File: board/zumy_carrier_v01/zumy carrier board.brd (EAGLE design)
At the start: 54 x 88.9 mm, 24 parts, among them IC1 SN74AUP2G17, IC2 SN74AUP2G17, J1 ODROID_POWER, J2 BATT_POWER, M1 POLOLU_STEP_DOWN, M2 ITG/MPU_MODULE, M3 POLOLU_DRV8833_MODULE, SW1 500SSP1S1M6QEA

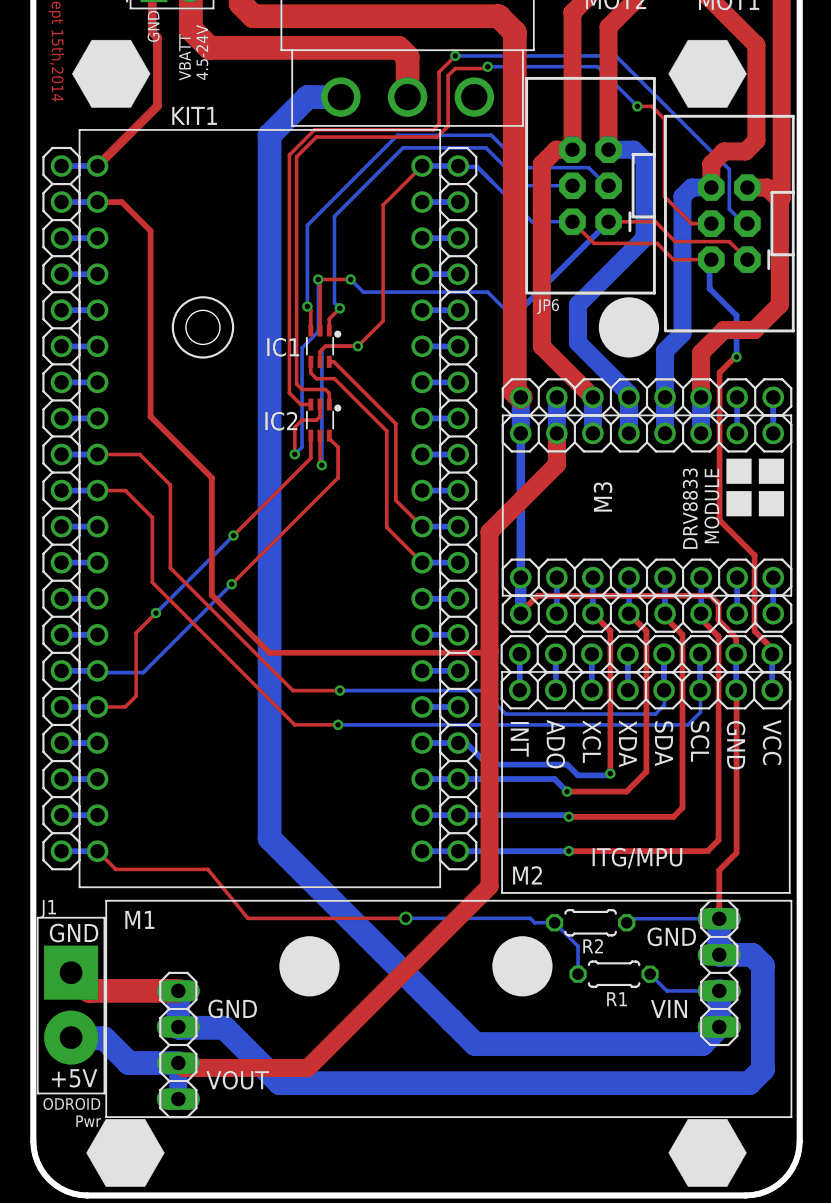
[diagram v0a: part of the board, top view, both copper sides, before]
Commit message: Added Rev. E Parts (5V Reg with UVLO, Cap on vsense, caps on level translators). Before ripup and rearrange.
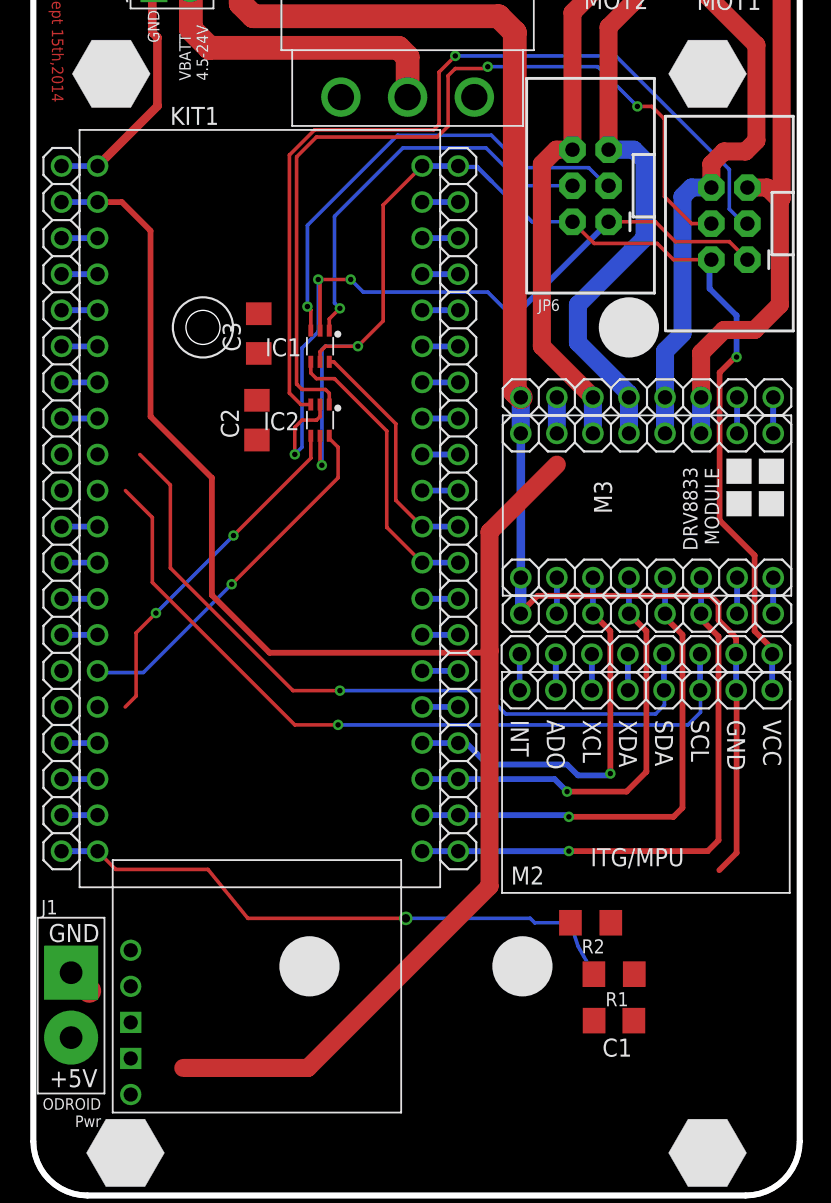
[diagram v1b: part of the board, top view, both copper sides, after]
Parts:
- removed M1: POLOLU_STEP_DOWN, zumy:POLOLU_STEP_DOWN
- added C1, C2, C3: 0.1uF, rcl:C1206
- added U$5: POLOLU_D24V50F5, zumy:POLOLU_D24V50F5
- R1: value (none) -> 200k; device resistor:0204/5 -> resistor:R1206
- R2: value (none) -> 100k; device resistor:0204/5 -> resistor:R1206
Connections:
- removed net N$35: JP5.7, KIT1.P$27
- removed net N$36: JP5.8, KIT1.P$28
- removed net N$39: JP5.11, KIT1.D+
- removed net N$40: JP5.12, KIT1.D-
- new net N$10: JP4.16, KIT1.P$16
- new net N$7: JP4.9, KIT1.P$9
- new net N$8: JP4.10, KIT1.P$10
- new net N$9: JP4.15, KIT1.P$15
- net +3V3: now also C2.1, C3.1
- net +5V: now also U$5.VOUT; no longer JP3.2, M1.VOUT1, M1.VOUT2, M3.VIN
- net GND: now also C1.2, C2.2, C3.2, U$5.GND1, U$5.GND2; no longer M1.GND1, M1.GND2, M1.GND3, M1.GND4
- net M2_ENCA_DIG: now also JP5.12, KIT1.D-; no longer JP4.15, KIT1.P$15
- net M2_ENCB_DIG: now also JP5.11, KIT1.D+; no longer JP4.16, KIT1.P$16
- net MPU_SCL: now also JP5.7, KIT1.P$27; no longer JP4.10, KIT1.P$10
- net MPU_SDA: now also JP5.8, KIT1.P$28; no longer JP4.9, KIT1.P$9
- net SW_VBATT: now also JP3.2, M3.VIN, U$5.VIN; no longer M1.VIN1, M1.VIN2
- net V_BATT_SENSE: now also C1.1
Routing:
- net SW_VBATT: track 102.4 -> 2.63 mm
- net GND: track 263.8 -> 188.5 mm
- net +5V: track 130.5 -> 114.4 mm
- net MPU_SDA: track 57.5 -> 54.3 mm
- net N$40: track 2.54 -> 0.00 mm
- net N$39: track 2.54 -> 0.00 mm
- net N$36: track 2.54 -> 0.00 mm
- net N$35: track 2.54 -> 0.00 mm
- net MPU_SCL: track 59.2 -> 57.0 mm
- net M2_ENCB_DIG: track 29.0 -> 27.1 mm
- net V_BATT_SENSE: track 41.3 -> 42.1 mm
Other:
- board text added: "A. Pullin A.J. Chen A.D. Buchan 2015"
- board text added: "Rev E"
- board text removed: "A. Pullin A.J. Chen 2014"
- board text removed: "Rev D"

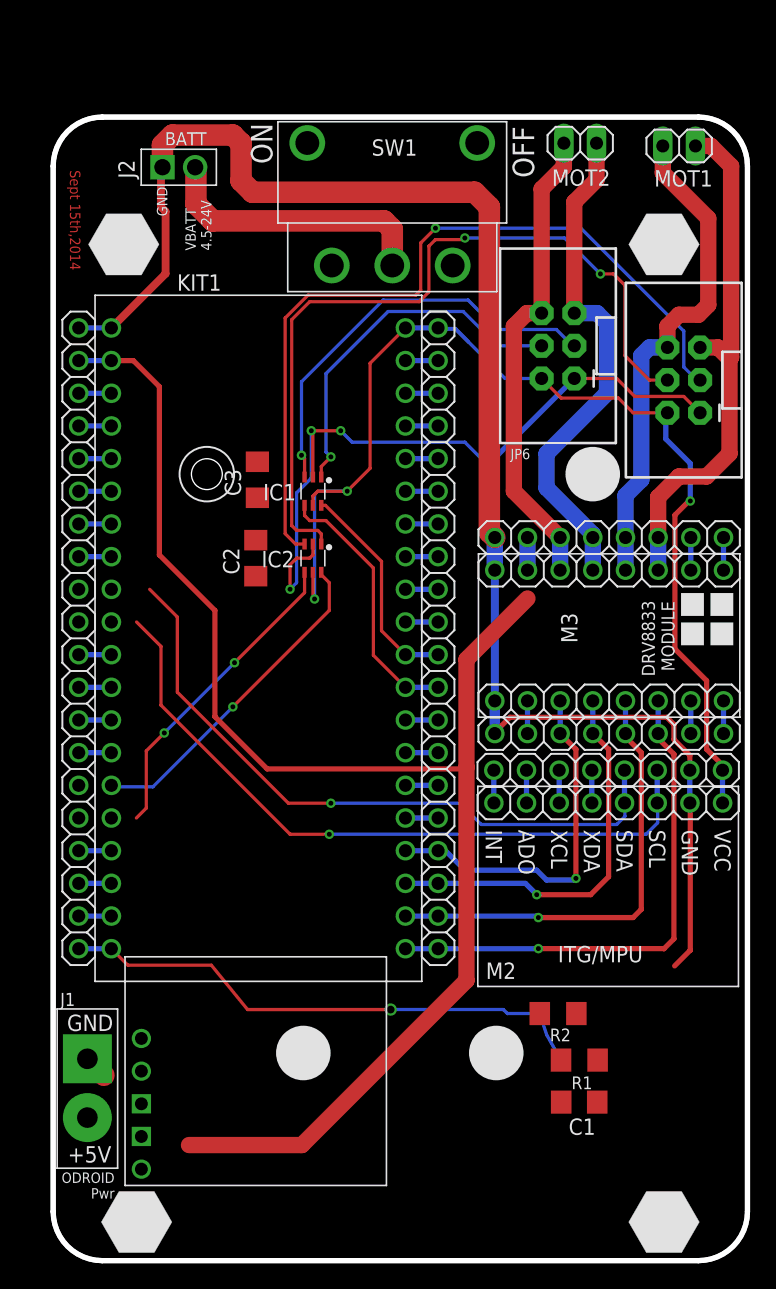
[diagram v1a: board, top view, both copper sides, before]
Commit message: Schematic and part placement mostly done. Need to clean up schematic, then fine adjust layout, then ready for routing.
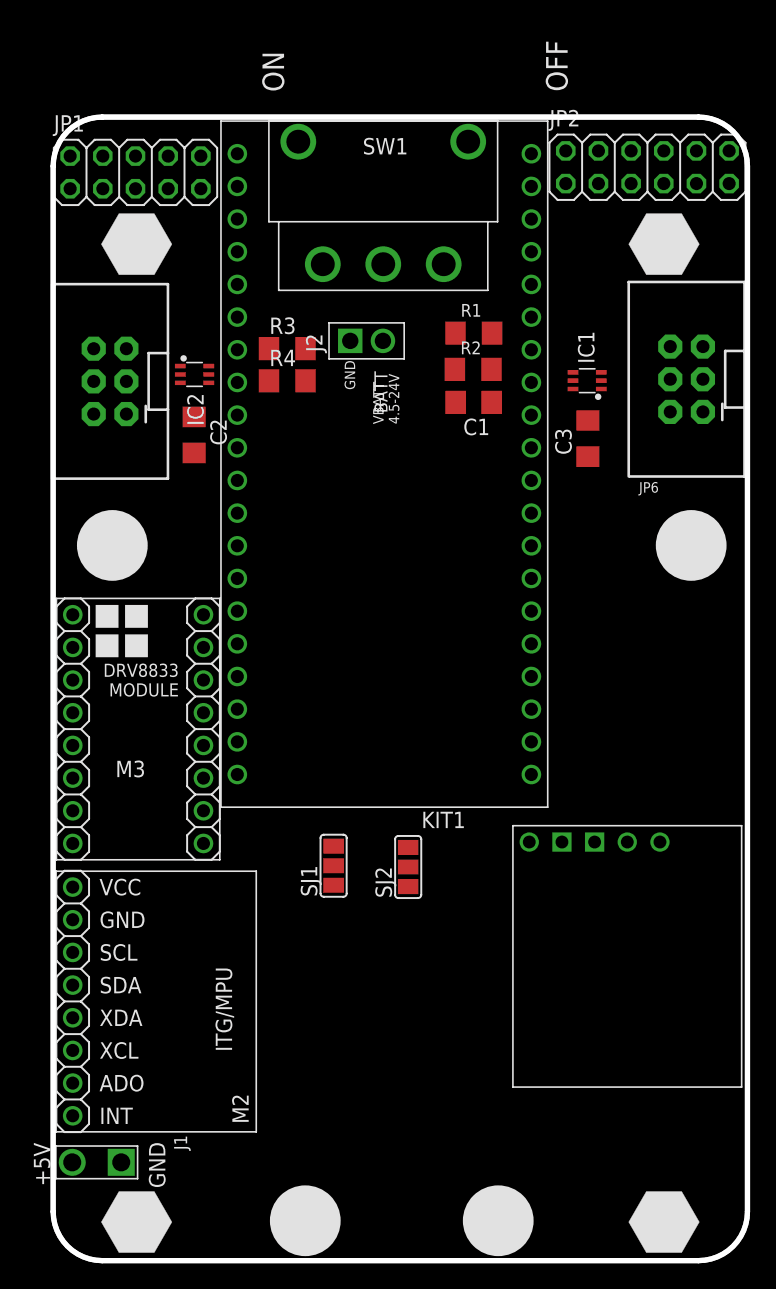
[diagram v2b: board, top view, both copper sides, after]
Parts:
- removed JP3: (no value), zumy:1X08
- removed JP4, JP5: (no value), zumy:1X20
- removed MOT1, MOT2: (no value), pinhead:1X02
- removed U$2, U$3: (no value), zumy:STANDOFF_POSITION
- added R3, R4: 2k2, resistor:R1206
- added SJ1, SJ2: (no value), SparkFun-Passives:SJ_2
- JP1: device zumy:1X08 -> pinhead:2X05
- JP2: device zumy:1X08 -> pinhead:2X06
- U$1: device zumy:STANDOFF_POSITION -> zumy:CHASSIS_STANDOFF
- moved JP1 59.2 mm to (6.40, 84.6)
- moved R1 57.1 mm to (32.7, 72.1), turned to 180 degrees
- moved C1 55.0 mm to (32.7, 66.7)
- moved R2 50.5 mm to (32.6, 69.3), turned to 0 degrees
- moved JP7 44.6 mm to (4.42, 68.4)
- moved JP2 44.1 mm to (46.2, 85.0)
- moved M3 41.5 mm to (13.0, 51.5), turned to 180 degrees
- moved U$5 41.1 mm to (35.7, 33.8), turned to 270 degrees
- moved M2 34.6 mm to (9.44, 20.2), turned to 90 degrees
- moved C3 25.9 mm to (41.6, 63.9)
- moved U$1 23.5 mm to (49.6, 55.6), turned to 180 degrees
- moved IC1 23.0 mm to (41.5, 68.4), turned to 90 degrees
- moved J2 19.9 mm to (23.1, 71.5)
- moved IC2 17.0 mm to (11.0, 68.9), turned to 270 degrees
- moved KIT1 16.7 mm to (25.7, 61.9), turned to 180 degrees
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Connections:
- removed net N$19: JP4.11, KIT1.P$11
- removed net N$20: JP4.12, KIT1.P$12
- removed net N$55: JP2.7, M3.NSLEEP
- removed net N$8: JP4.10, KIT1.P$10
- removed net N$9: JP4.15, KIT1.P$15
- new net MBED_SCL: KIT1.P$27, R3.1
- new net MBED_SDA: KIT1.P$28, R4.1
- new net N$17: KIT1.VIN, SJ2.2
- new net N$5: KIT1.D-
- new net N$6: KIT1.D+
- new net NSLEEP: KIT1.P$8, M3.NSLEEP
- net +3V3: now also R3.2, R4.2; no longer JP1.8, JP5.20
- net +5V: now also SJ1.3, SJ2.3; no longer JP4.2, KIT1.VIN
- net AIN1: no longer JP2.6, JP5.1
- net AIN2: no longer JP2.5, JP5.2
- net BIN1: no longer JP2.3, JP5.4
- net BIN2: no longer JP2.4, JP5.3
- net GND: no longer JP1.7, JP2.1, JP3.1, JP4.1
- net M1_ENCA_DIG: now also KIT1.P$11; no longer JP5.10, KIT1.P$30
- net M1_ENCB_DIG: now also KIT1.P$12; no longer JP5.9, KIT1.P$29
- net M2_ENCA_DIG: now also KIT1.P$30; no longer JP5.12, KIT1.D-
- net M2_ENCB_DIG: now also KIT1.P$29; no longer JP5.11, KIT1.D+
- net MOTOR1_OUTA: no longer JP3.5, MOT1.1
- net MOTOR1_OUTB: no longer JP3.6, MOT1.2
- net MOTOR2_OUTA: no longer JP3.3, MOT2.1
- net MOTOR2_OUTB: no longer JP3.4, MOT2.2
- net MPU_SCL: now also KIT1.P$10; no longer JP1.6, JP5.7, KIT1.P$27
- net MPU_SDA: now also KIT1.P$9; no longer JP1.5, JP5.8, KIT1.P$28
- net N$1: no longer JP1.1
- net N$10: no longer JP4.16
- net N$11: no longer JP4.3
- net N$12: no longer JP4.4
- net N$13: no longer JP4.5
- net N$14: no longer JP4.6
- net N$15: no longer JP4.7
- net N$16: now also M3.VIN, SJ1.2; no longer JP4.8, KIT1.P$8
- net N$2: no longer JP1.2
- net N$21: no longer JP4.13
- net N$22: no longer JP4.14
- net N$25: no longer JP4.17
- net N$26: no longer JP4.18
- net N$27: no longer JP4.19
- net N$3: no longer JP1.3
- net N$33: no longer JP5.5
- net N$34: no longer JP5.6
- net N$4: no longer JP1.4
- net N$41: no longer JP5.13
- net N$42: no longer JP5.14
- net N$43: no longer JP5.15
- net N$44: no longer JP5.16
- net N$45: no longer JP5.17
- net N$46: no longer JP5.18
- net N$47: no longer JP5.19
- net N$50: no longer JP2.2
- net N$56: no longer JP2.8
- net N$63: no longer JP3.7
- net N$64: no longer JP3.8
- net N$7: now also KIT1.P$20; no longer JP4.9, KIT1.P$9
- net SW_VBATT: now also SJ1.1, SJ2.1, SW1.3; no longer JP3.2, M3.VIN, SW1.1
- net V_BATT_SENSE: now also KIT1.P$15; no longer JP4.20, KIT1.P$20
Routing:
- net GND: track 188.5 -> 0.00 mm, vias 3 -> 0
- net +5V: track 114.4 -> 0.00 mm
- net +3V3: track 87.4 -> 0.00 mm, vias 3 -> 0
- net MOTOR2_ENCB: track 62.4 -> 0.00 mm, vias 1 -> 0
- net MOTOR2_ENCA: track 61.1 -> 0.00 mm, vias 2 -> 0
- net MPU_SCL: track 57.0 -> 0.00 mm, vias 1 -> 0
- net MPU_SDA: track 54.3 -> 0.00 mm, vias 1 -> 0
- net V_BATT_SENSE: track 42.1 -> 0.00 mm, vias 1 -> 0
- net MOTOR1_OUTB: track 41.1 -> 0.00 mm
- net AIN1: track 40.2 -> 0.00 mm, vias 1 -> 0
- net MOTOR2_OUTB: track 39.4 -> 0.00 mm
- net MOTOR1_OUTA: track 38.8 -> 0.00 mm
- net MOTOR2_OUTA: track 37.0 -> 0.00 mm
- net AIN2: track 35.4 -> 0.00 mm, vias 1 -> 0
- net BIN2: track 33.1 -> 0.00 mm, vias 1 -> 0
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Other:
- board text added: "A. Pullin A.J. Chen A.D. Buchan Aug. 2015"
- board text added: "ZUMY"
- board text removed: "A. Pullin A.J. Chen A.D. Buchan 2015"
- board text removed: "ODROID Pwr"
- board text removed: "Sept 15th,2014"

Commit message: First pass at layout done
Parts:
- removed JP6, JP7: (no value), SparkFun-Connectors:2X3-SHROUDED
- removed M3: POLOLU_DRV8833_MODULE, zumy:POLOLU_DRV8833_MODULE
- added M1: (no value), SparkFun-Connectors:2X3-SHROUDED
- added MOT_DRIVE: POLOLU_DRV8833_MODULE, zumy:POLOLU_DRV8833_MODULE
- added MPU: ITG/MPU_MODULE, zumy:ITG/MPU_MODULE
- M2: value ITG/MPU_MODULE -> (none); device zumy:ITG/MPU_MODULE -> SparkFun-Connectors:2X3-SHROUDED
- moved JP1 115.5 mm to (-40.5, -21.0), turned to 90 degrees
- moved JP2 107.8 mm to (-40.5, 21.0), turned to 90 degrees
- moved IC1 106.4 mm to (-22.0, -17.0), turned to 0 degrees
- moved C3 101.1 mm to (-19.0, -17.0), turned to 270 degrees
- moved SW1 97.4 mm to (-33.4, 0.00), turned to 90 degrees
- moved J2 90.7 mm to (-29.2, -2.60), turned to 90 degrees
- moved R3 90.2 mm to (-27.0, -7.20), turned to 90 degrees
- moved R1 89.7 mm to (-28.0, 6.00), turned to 270 degrees
- moved R4 86.8 mm to (-24.4, -7.20), turned to 90 degrees
- moved R2 85.6 mm to (-25.0, 6.00), turned to 90 degrees
- moved C1 81.7 mm to (-22.0, 6.00), turned to 270 degrees
- moved KIT1 75.8 mm to (-18.0, 0.00), turned to 270 degrees
- moved U$1 68.5 mm to (-10.4, 22.5), turned to 270 degrees
- moved U$5 66.3 mm to (14.4, -29.0), turned to 0 degrees
- moved IC2 61.5 mm to (-22.0, 17.0), turned to 180 degrees
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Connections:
- net N$11 renamed VB
- net N$12 renamed NR
- net N$47 renamed VU
- net VBATT renamed N$2
- net V_BATT_SENSE renamed BATT_SENSE
- removed net AIN1: KIT1.P$21, M3.AIN1
- removed net AIN2: KIT1.P$22, M3.AIN2
- removed net BIN1: KIT1.P$24, M3.BIN1
- removed net BIN2: KIT1.P$23, M3.BIN2
- removed net M1_ENCA_DIG: IC1.6, KIT1.P$11
- removed net M1_ENCB_DIG: IC1.4, KIT1.P$12
- removed net M2_ENCA_DIG: IC2.6, KIT1.P$30
- removed net M2_ENCB_DIG: IC2.4, KIT1.P$29
- removed net MOTOR1_ENCA: IC1.1, JP6.4
- removed net MOTOR1_ENCB: IC1.3, JP6.3
- removed net MOTOR1_OUTA: JP7.6, M3.AOUT2
- removed net MOTOR1_OUTB: JP7.5, M3.AOUT1
- removed net MOTOR2_ENCA: IC2.1, JP7.4
- removed net MOTOR2_ENCB: IC2.3, JP7.3
- removed net MOTOR2_OUTA: JP6.6, M3.BOUT1
- removed net MOTOR2_OUTB: JP6.5, M3.BOUT2
- removed net N$1 (its old number): M2.INT
- removed net N$10: KIT1.P$16
- removed net N$13: KIT1.P$5
- removed net N$14: KIT1.P$6
- removed net N$15: KIT1.P$7
- removed net N$16: M3.VIN, SJ1.2
- removed net N$2 (its old number): M2.ADO
- removed net N$21: KIT1.P$13
- removed net N$22: KIT1.P$14
- removed net N$25: KIT1.P$17
- removed net N$26: KIT1.P$18
- removed net N$27: KIT1.P$19
- removed net N$33: KIT1.P$25
- removed net N$34: KIT1.P$26
- removed net N$4: M2.XDA
- removed net N$41: KIT1.TD+
- removed net N$42: KIT1.TD-
- removed net N$43: KIT1.RD+
- removed net N$44: KIT1.RD-
- removed net N$45: KIT1.IF+
- removed net N$46: KIT1.IF-
- removed net N$5: KIT1.D-
- removed net N$50: M3.VMM
- removed net N$56: M3.NFAULT
- removed net N$6: KIT1.D+
- removed net N$63: M3.AISEN
- removed net N$64: M3.BISEN
- removed net N$7: KIT1.P$20
- removed net NSLEEP: KIT1.P$8, M3.NSLEEP
- removed net SW_VBATT: R1.2, SJ1.1, SJ2.1, SW1.3, U$5.VIN
- new net M1_EA: IC1.1, M1.4
- new net M1_EAD: IC1.6, KIT1.P$29
- new net M1_EB: IC1.3, M1.3
- new net M1_EBD: IC1.4, KIT1.P$30
- new net M1_IN1: KIT1.P$21, MOT_DRIVE.AIN1
- new net M1_IN2: KIT1.P$22, MOT_DRIVE.AIN2
- new net M1_OUT1: M1.6, MOT_DRIVE.AOUT1
- new net M1_OUT2: M1.5, MOT_DRIVE.AOUT2
- new net M2_EA: IC2.1, M2.4
- new net M2_EAD: IC2.6, KIT1.P$11
- new net M2_EB: IC2.3, M2.3
- new net M2_EBD: IC2.4, KIT1.P$12
- new net M2_IN1: KIT1.P$24, MOT_DRIVE.BIN1
- new net M2_IN2: KIT1.P$23, MOT_DRIVE.BIN2
- new net M2_OUT1: M2.6, MOT_DRIVE.BOUT1
- new net M2_OUT2: M2.5, MOT_DRIVE.BOUT2
- new net MBED_A0: JP2.12, KIT1.P$16
- new net MBED_A1: JP2.10, KIT1.P$17
- new net MBED_A2: JP2.8, KIT1.P$18
- new net MBED_A3: JP2.6, KIT1.P$19
- new net MBED_MISO: JP2.9, KIT1.P$6
- new net MBED_MOSI: JP2.11, KIT1.P$5
- new net MBED_PWM0: JP1.6, KIT1.P$25
- new net MBED_PWM1: JP1.5, KIT1.P$26
- new net MBED_RX: JP1.4, KIT1.P$14
- new net MBED_SCK: JP2.7, KIT1.P$7
- new net MBED_SS: JP2.5, KIT1.P$20
- new net MBED_TX: JP1.2, KIT1.P$13
- new net M_SLEEP: KIT1.P$8, MOT_DRIVE.NSLEEP
- new net V+: JP2.4, R1.2, SJ1.1, SJ2.3, SW1.3, U$5.VIN
- net +3V3: now also JP2.3, M1.2, M2.2, MPU.VCC; no longer JP6.2, JP7.2, M2.VCC
- net +5V: now also JP1.7, JP1.8, JP2.2, SJ2.1; no longer SJ2.3
- net GND: now also JP1.10, JP1.9, JP2.1, M1.1, M2.1, MOT_DRIVE.GND1, MOT_DRIVE.GND2, MPU.GND; no longer JP6.1, JP7.1, M2.GND, M3.GND1, M3.GND2
- net MBED_SCL: now also JP1.3
- net MBED_SDA: now also JP1.1
- net MPU_SCL: now also MPU.SCL; no longer M2.SCL
- net MPU_SDA: now also MPU.SDA; no longer M2.SDA
- net N$3: now also MOT_DRIVE.VIN, SJ1.2; no longer M2.XCL
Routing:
- net +5V: track 0.00 -> 159.9 mm, vias 0 -> 1
- net +3V3: track 0.00 -> 142.9 mm, vias 0 -> 3
- net V+: track 0.00 -> 97.9 mm, vias 0 -> 1
- net M2_OUT2: track 0.00 -> 77.7 mm, vias 0 -> 1
- net M2_OUT1: track 0.00 -> 74.1 mm, vias 0 -> 1
- net MBED_TX: track 0.00 -> 56.2 mm
- net MBED_RX: track 0.00 -> 55.6 mm
- net M1_IN2: track 0.00 -> 44.1 mm
- net M1_IN1: track 0.00 -> 44.1 mm
- net M2_IN1: track 0.00 -> 43.9 mm
- net M2_IN2: track 0.00 -> 43.9 mm
- net MBED_MOSI: track 0.00 -> 42.7 mm, vias 0 -> 1
- net MBED_MISO: track 0.00 -> 39.6 mm, vias 0 -> 1
- net MBED_SCK: track 0.00 -> 37.7 mm, vias 0 -> 1
- net M_SLEEP: track 0.00 -> 32.2 mm
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- added copper zone on layer 1, net GND
- added copper zone on layer 16, net GND
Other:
- board size 54 x 88.9 mm -> 90 x 60 mm
